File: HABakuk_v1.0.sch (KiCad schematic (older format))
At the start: 57 parts, among them J1 ICSP, J10 C-, J2 I2C, J3 SERIAL, J4 GPS_Ant, J5 ANT_UP, J6 ANT_DWN, J7 SOL+, J8 SOL-, J9 C+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

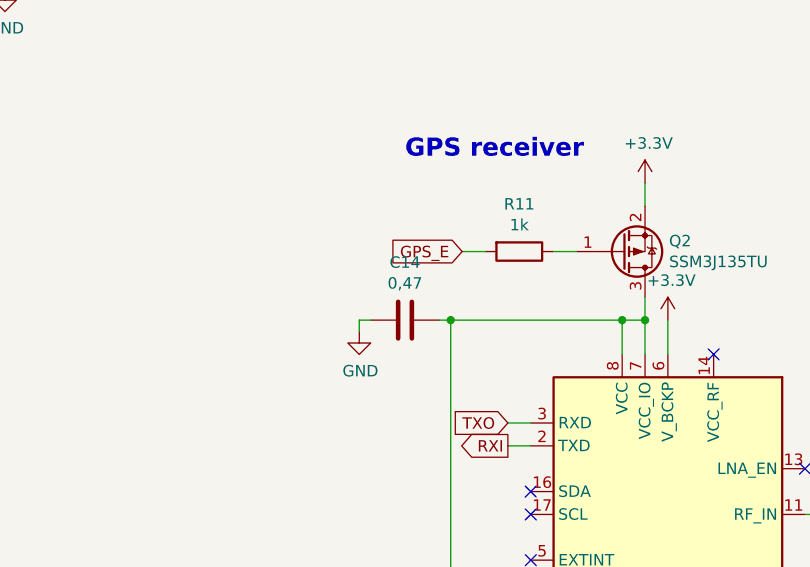
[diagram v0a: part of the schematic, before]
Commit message: Added BOMs, modified 8 MHz crystal footprint
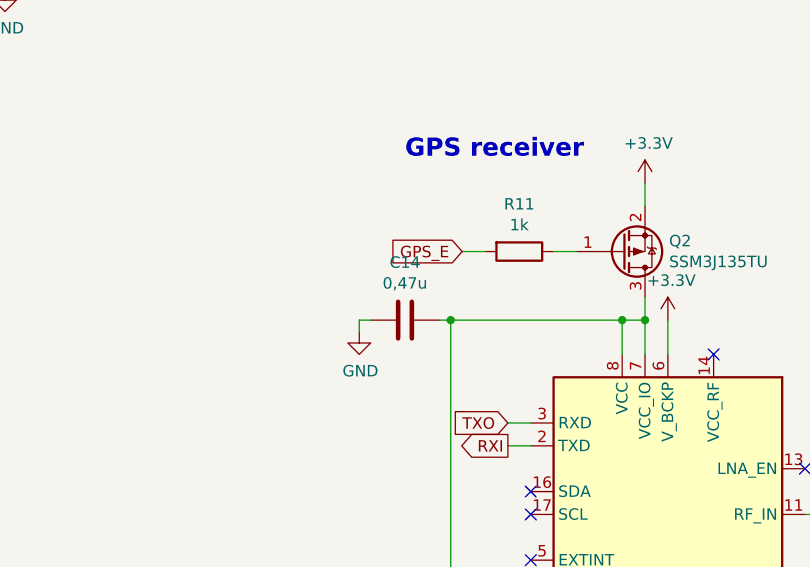
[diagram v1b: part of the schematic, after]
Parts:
- C14: value 0,47 -> 0,47u
- Y1: footprint Crystal:Crystal_SMD_Abracon_ABM8G-4Pin_3.2x2.5mm -> Crystal:Crystal_SMD_5032-4Pin_5.0x3.2mm
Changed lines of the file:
@@
 F 0 "Y1" V 7754 2894 50  0000 L CNN
 F 1 "Crystal_GND24_Small" V 7845 2894 50  0000 L CNN
-F 2 "Crystal:Crystal_SMD_Abracon_ABM8G-4Pin_3.2x2.5mm" H 7800 2750 50  0001 C CNN
+F 2 "Crystal:Crystal_SMD_5032-4Pin_5.0x3.2mm" H 7800 2750 50  0001 C CNN
 F 3 "~" H 7800 2750 50  0001 C CNN
 	1    7800 2750
@@
 P 5000 3900
 F 0 "C14" V 4748 3900 50  0000 C CNN
-F 1 "0,47" V 4839 3900 50  0000 C CNN
+F 1 "0,47u" V 4839 3900 50  0000 C CNN
 F 2 "Capacitor_SMD:C_0603_1608Metric" H 5038 3750 50  0001 C CNN
 F 3 "~" H 5000 3900 50  0001 C CNN
